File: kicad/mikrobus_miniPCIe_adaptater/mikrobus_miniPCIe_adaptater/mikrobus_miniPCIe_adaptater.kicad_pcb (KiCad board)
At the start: 2 copper layers, 35.4 x 59.7 mm, 4 parts, among them IC101 MIKROE-924, J101 Bus_PCI_Express_Mini

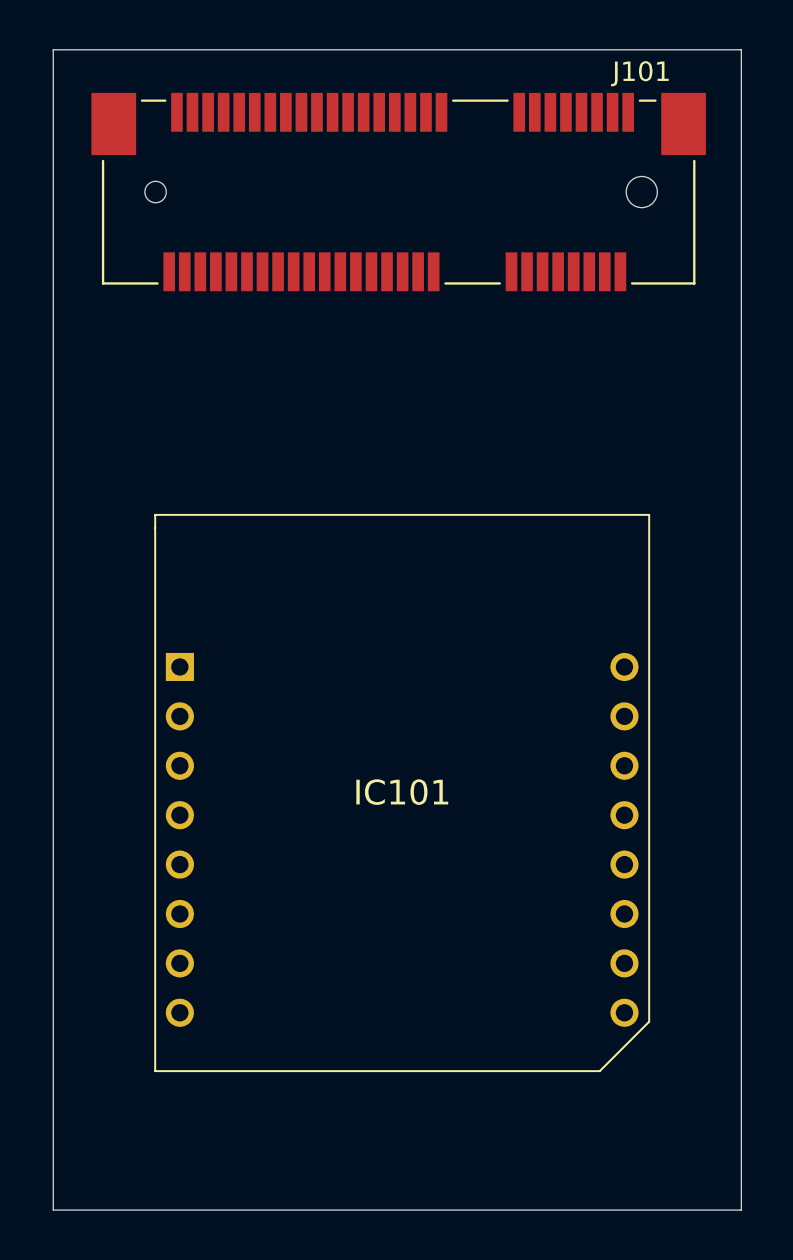
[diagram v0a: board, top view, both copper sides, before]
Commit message: add power and gnd
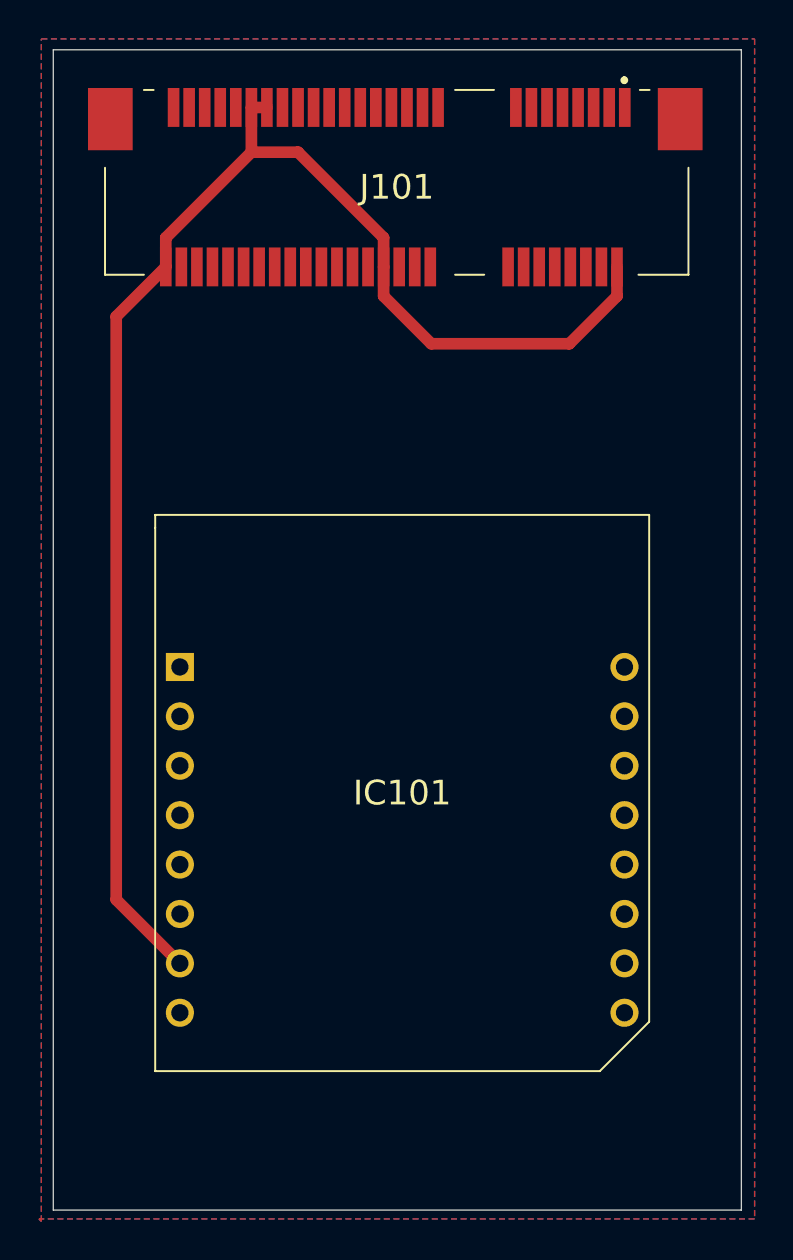
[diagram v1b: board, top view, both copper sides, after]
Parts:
- J101: value Bus_PCI_Express_Mini -> 1717831-1; footprint Connector_PCBEdge:BUS_PCI_Express_Mini -> Mini_PCI_e:17178311
- moved J101 0.27 mm to (111.5, 71.2)
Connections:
- IC101 pad 7: VCC -> 3.3V
- J101 pad 15: Net-(J101-GND-Pad15) -> GND
- J101 pad 18: Net-(J101-GND-Pad15) -> GND
- J101 pad 2: unconnected-(J101-+3V3AUX-Pad2) -> 3.3V
- J101 pad 21: Net-(J101-GND-Pad15) -> GND
- J101 pad 24: unconnected-(J101-+3V3AUX-Pad24) -> 3.3V
- J101 pad 26: Net-(J101-GND-Pad15) -> GND
- J101 pad 27: Net-(J101-GND-Pad15) -> GND
- J101 pad 29: Net-(J101-GND-Pad15) -> GND
- J101 pad 34: Net-(J101-GND-Pad15) -> GND
- J101 pad 35: Net-(J101-GND-Pad15) -> GND
- J101 pad 37: Net-(J101-GND-Pad15) -> GND
- J101 pad 39: unconnected-(J101-+3V3AUX-Pad39) -> 3.3V
- J101 pad 4: Net-(J101-GND-Pad15) -> GND
- J101 pad 40: Net-(J101-GND-Pad15) -> GND
- J101 pad 41: unconnected-(J101-+3V3AUX-Pad41) -> 3.3V
- J101 pad 43: Net-(J101-GND-Pad15) -> GND
- J101 pad 50: Net-(J101-GND-Pad15) -> GND
- J101 pad 52: unconnected-(J101-+3V3AUX-Pad52) -> 3.3V
- J101 pad 9: Net-(J101-GND-Pad15) -> GND
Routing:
- net 3.3V: track 0.00 -> 76.2 mm
- added copper zone on B.Cu, net GND
- added copper zone on F.Cu, net GND
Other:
- board text added: "AN"
- board text added: "CS"
- board text added: "INT"
- board text added: "MISO"
- board text added: "MOSI"
- board text added: "PWM"
- board text added: "RST"
- board text added: "RX"
- board text added: "SCK"
- board text added: "SCL"
- board text added: "SDA"
- board text added: "TX"
- board text removed: "CS/GP8"
- board text removed: "GP14/TX"
- board text removed: "GP15/RX"
- board text removed: "GP17/INT"
- board text removed: "GP18/PWM"
- board text removed: "GP2(0)/SDA"
- board text removed: "GP22"
- board text removed: "GP3(1)/SCL"
- board text removed: "MISO/GP9"
- board text removed: "MOSI/GP10"
- board text removed: "RST/GP4"
- board text removed: "SCK/GP11"
